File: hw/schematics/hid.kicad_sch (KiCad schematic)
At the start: 114 parts, among them M1 SK8701-01-004-MODULE, M2 SK8701-01-004-SENSOR, SW1 SW_Push, SW10 SW_Push, SW11 SW_Push, SW12 SW_Push, SW13 SW_Push, SW14 SW_Push, SW15 SW_Push, SW16 SW_Push, SW17 SW_Push, SW18 SW_Push, SW19 SW_Push, SW2 SW_Push, SW20 SW_Push, SW21 SW_Push, SW22 SW_Push, SW23 SW_Push, SW3 SW_Push, SW4 SW_Push, SW5 SW_Push, SW6 SW_Push, SW7 SW_Push, SW8 SW_Push, SW9 SW_Push

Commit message: apply 0603 footprint
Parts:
- R10, R11, R12, R18, R19, R20, R21, R8, R9, rR10, rR11, rR12, rR18, rR19, rR20, rR21, rR8, rR9: footprint (none) -> Alidade:SMD_0603
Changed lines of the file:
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@@
 			)
 		)
-		(property "Footprint" ""
+		(property "Footprint" "Alidade:SMD_0603"
 			(at 248.92 217.17 0)
 			(effects
@@
 			)
 		)
-		(property "Footprint" ""
+		(property "Footprint" "Alidade:SMD_0603"
 			(at 378.46 102.87 0)
 			(effects
@@
 			)
 		)
-		(property "Footprint" ""
+		(property "Footprint" "Alidade:SMD_0603"
 			(at 248.92 219.71 0)
 			(effects
@@
 			)
 		)
-		(property "Footprint" ""
+		(property "Footprint" "Alidade:SMD_0603"
 			(at 248.92 222.25 0)
 			(effects
@@
 			)
 		)
-		(property "Footprint" ""
+		(property "Footprint" "Alidade:SMD_0603"
 			(at 43.18 118.11 0)
 			(effects
@@
 			)
 		)
-		(property "Footprint" ""
+		(property "Footprint" "Alidade:SMD_0603"
 			(at 43.18 72.39 0)
 			(effects
@@
 			)
 		)
-		(property "Footprint" ""
+		(property "Footprint" "Alidade:SMD_0603"
 			(at 173.99 204.47 0)
 			(effects
@@
 			)
 		)
-		(property "Footprint" ""
+		(property "Footprint" "Alidade:SMD_0603"
 			(at 180.34 204.47 0)
 			(effects
@@
 			)
 		)
-		(property "Footprint" ""
+		(property "Footprint" "Alidade:SMD_0603"
 			(at 43.18 87.63 0)
 			(effects
@@
 			)
 		)
-		(property "Footprint" ""
+		(property "Footprint" "Alidade:SMD_0603"
 			(at 176.53 222.25 0)
 			(effects
@@
 			)
 		)
-		(property "Footprint" ""
+		(property "Footprint" "Alidade:SMD_0603"
 			(at 176.53 219.71 0)
 			(effects
@@
 			)
 		)
-		(property "Footprint" ""
+		(property "Footprint" "Alidade:SMD_0603"
 			(at 378.46 118.11 0)
 			(effects
@@
 			)
 		)
-		(property "Footprint" ""
+		(property "Footprint" "Alidade:SMD_0603"
 			(at 43.18 102.87 0)
 			(effects
@@
 			)
 		)
-		(property "Footprint" ""
+		(property "Footprint" "Alidade:SMD_0603"
 			(at 252.73 204.47 0)
 			(effects
@@
 			)
 		)
-		(property "Footprint" ""
+		(property "Footprint" "Alidade:SMD_0603"
 			(at 246.38 204.47 0)
 			(effects
@@
 			)
 		)
-		(property "Footprint" ""
+		(property "Footprint" "Alidade:SMD_0603"
 			(at 176.53 217.17 0)
 			(effects
@@
 			)
 		)
-		(property "Footprint" ""
+		(property "Footprint" "Alidade:SMD_0603"
 			(at 378.46 87.63 0)
 			(effects
@@
 			)
 		)
-		(property "Footprint" ""
+		(property "Footprint" "Alidade:SMD_0603"
 			(at 378.46 72.39 0)
 			(effects

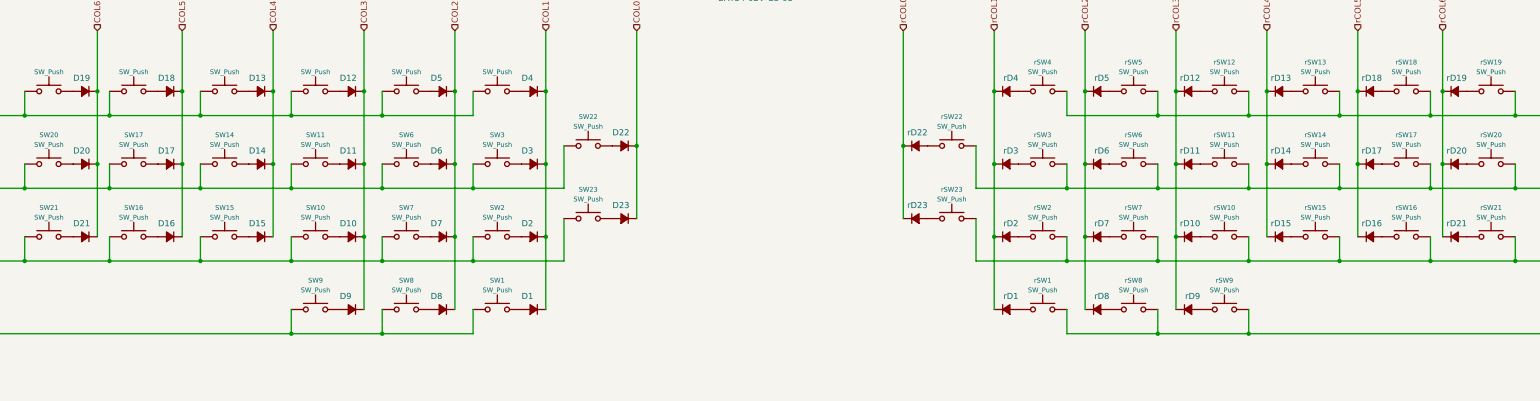
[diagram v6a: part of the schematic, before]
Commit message: Use bat54 instead
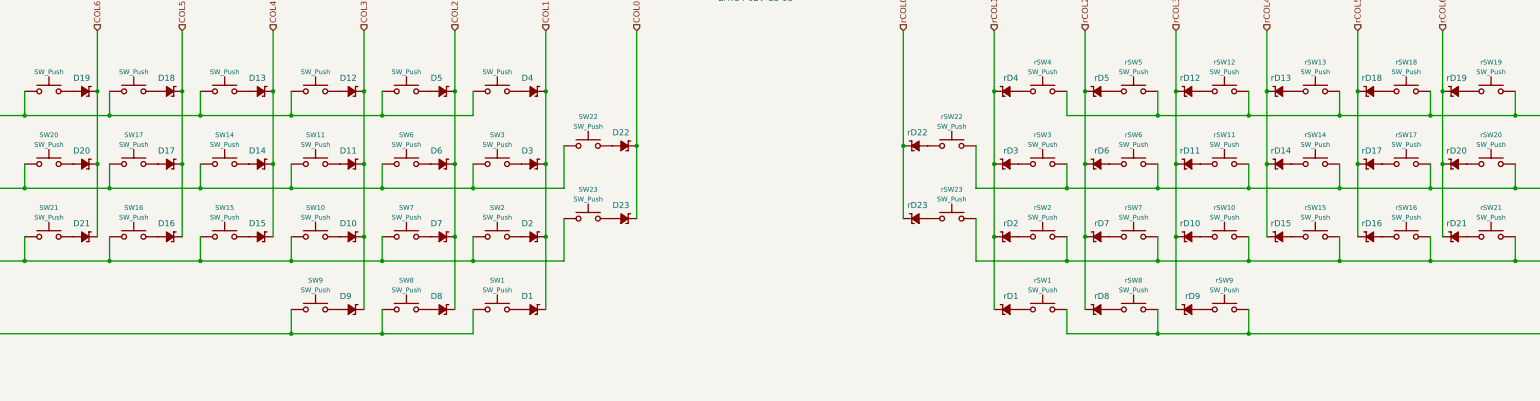
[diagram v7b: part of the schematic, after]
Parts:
- D1, D10, D11, D12, D13, D14, D15, D16, D17, D18, D19, D2, D20, D21, D22, D23, D3, D4, D5, D6, D7, D8, D9, rD1, rD10, rD11, rD12, rD13, rD14, rD15, rD16, rD17, rD18, rD19, rD2, rD20, rD21, rD22, rD23, rD3, rD4, rD5, rD6, rD7, rD8, rD9: value BAT54-02V-G3-08 -> BAT54; footprint Alidade:SOD-523 -> Alidade:SOT23; symbol Alidade:D -> Alidade:BAT54; LCSC Part # (none) -> C8590
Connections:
- net COL0: now also D22.3 (K), D23.3 (K); no longer D22.1 (K), D23.1 (K)
- net COL1: now also D1.3 (K), D2.3 (K), D3.3 (K), D4.3 (K); no longer D1.1 (K), D2.1 (K), D3.1 (K), D4.1 (K)
- net COL2: now also D5.3 (K), D6.3 (K), D7.3 (K), D8.3 (K); no longer D5.1 (K), D6.1 (K), D7.1 (K), D8.1 (K)
- net COL3: now also D10.3 (K), D11.3 (K), D12.3 (K), D9.3 (K); no longer D10.1 (K), D11.1 (K), D12.1 (K), D9.1 (K)
- net COL4: now also D13.3 (K), D14.3 (K), D15.3 (K); no longer D13.1 (K), D14.1 (K), D15.1 (K)
- net COL5: now also D16.3 (K), D17.3 (K), D18.3 (K); no longer D16.1 (K), D17.1 (K), D18.1 (K)
- net COL6: now also D19.3 (K), D20.3 (K), D21.3 (K); no longer D19.1 (K), D20.1 (K), D21.1 (K)
- net rCOL0: now also rD22.3 (K), rD23.3 (K); no longer rD22.1 (K), rD23.1 (K)
- net rCOL1: now also rD1.3 (K), rD2.3 (K), rD3.3 (K), rD4.3 (K); no longer rD1.1 (K), rD2.1 (K), rD3.1 (K), rD4.1 (K)
- net rCOL2: now also rD5.3 (K), rD6.3 (K), rD7.3 (K), rD8.3 (K); no longer rD5.1 (K), rD6.1 (K), rD7.1 (K), rD8.1 (K)
- net rCOL3: now also rD10.3 (K), rD11.3 (K), rD12.3 (K), rD9.3 (K); no longer rD10.1 (K), rD11.1 (K), rD12.1 (K), rD9.1 (K)
- net rCOL4: now also rD13.3 (K), rD14.3 (K), rD15.3 (K); no longer rD13.1 (K), rD14.1 (K), rD15.1 (K)
- net rCOL5: now also rD16.3 (K), rD17.3 (K), rD18.3 (K); no longer rD16.1 (K), rD17.1 (K), rD18.1 (K)
- net rCOL6: now also rD19.3 (K), rD20.3 (K), rD21.3 (K); no longer rD19.1 (K), rD20.1 (K), rD21.1 (K)
- net at rSW4.2: now also rD4.1 (A); no longer rD4.2 (A)
- net at rSW6.2: now also rD6.1 (A); no longer rD6.2 (A)
- net at SW7.2: now also D7.1 (A); no longer D7.2 (A)
- net at SW23.1: now also D23.1 (A); no longer D23.2 (A)
- net at SW18.2: now also D18.1 (A); no longer D18.2 (A)
- net at SW13.2: now also D13.1 (A); no longer D13.2 (A)
- net at SW10.2: now also D10.1 (A); no longer D10.2 (A)
- net at rSW16.2: now also rD16.1 (A); no longer rD16.2 (A)
- net at rSW20.2: now also rD20.1 (A); no longer rD20.2 (A)
- net at SW9.2: now also D9.1 (A); no longer D9.2 (A)
- net at rSW8.2: now also rD8.1 (A); no longer rD8.2 (A)
- net at rSW5.2: now also rD5.1 (A); no longer rD5.2 (A)
- net at rSW14.2: now also rD14.1 (A); no longer rD14.2 (A)
- net at SW1.2: now also D1.1 (A); no longer D1.2 (A)
- net at rSW15.2: now also rD15.1 (A); no longer rD15.2 (A)
- net at rSW13.2: now also rD13.1 (A); no longer rD13.2 (A)
- net at SW12.2: now also D12.1 (A); no longer D12.2 (A)
- net at SW16.2: now also D16.1 (A); no longer D16.2 (A)
- net at rSW10.2: now also rD10.1 (A); no longer rD10.2 (A)
- net at rSW1.2: now also rD1.1 (A); no longer rD1.2 (A)
- net at SW3.2: now also D3.1 (A); no longer D3.2 (A)
- net at rSW21.2: now also rD21.1 (A); no longer rD21.2 (A)
- net at SW22.1: now also D22.1 (A); no longer D22.2 (A)
- net at SW6.2: now also D6.1 (A); no longer D6.2 (A)
- net at SW21.2: now also D21.1 (A); no longer D21.2 (A)
- net at rSW17.2: now also rD17.1 (A); no longer rD17.2 (A)
- net at SW14.2: now also D14.1 (A); no longer D14.2 (A)
- net at rSW9.2: now also rD9.1 (A); no longer rD9.2 (A)
- net at SW4.2: now also D4.1 (A); no longer D4.2 (A)
- net at rSW19.2: now also rD19.1 (A); no longer rD19.2 (A)
- net at rSW18.2: now also rD18.1 (A); no longer rD18.2 (A)
- net at rSW2.2: now also rD2.1 (A); no longer rD2.2 (A)
- net at SW19.2: now also D19.1 (A); no longer D19.2 (A)
- net at SW11.2: now also D11.1 (A); no longer D11.2 (A)
- net at SW5.2: now also D5.1 (A); no longer D5.2 (A)
- net at SW20.2: now also D20.1 (A); no longer D20.2 (A)
- net at rSW23.1: now also rD23.1 (A); no longer rD23.2 (A)
- net at rSW22.1: now also rD22.1 (A); no longer rD22.2 (A)
- net at SW2.2: now also D2.1 (A); no longer D2.2 (A)
- net at rSW7.2: now also rD7.1 (A); no longer rD7.2 (A)
- net at SW8.2: now also D8.1 (A); no longer D8.2 (A)
- net at SW17.2: now also D17.1 (A); no longer D17.2 (A)
- net at rSW3.2: now also rD3.1 (A); no longer rD3.2 (A)
- net at rSW11.2: now also rD11.1 (A); no longer rD11.2 (A)
- net at rSW12.2: now also rD12.1 (A); no longer rD12.2 (A)
- net at SW15.2: now also D15.1 (A); no longer D15.2 (A)

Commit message: add some LCSC part numbers
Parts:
- R10, R11, R12, rR10, rR11, rR12: footprint Alidade:SMD_0603 -> Alidade:0603; LCSC Part # (none) -> C21189
- R18, R19, R20, R21, R8, R9, rR18, rR19, rR20, rR21, rR8, rR9: footprint Alidade:SMD_0603 -> Alidade:0603; LCSC Part # (none) -> C25804
